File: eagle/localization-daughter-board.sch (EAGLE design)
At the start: 7 parts, among them U1 LM340MP-5.0/NOPB, U2 STM32F042FXP

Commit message: Just saving progress
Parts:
- added J2: (no value), SparkFun-Connectors:CONN_05JST-VERT
- added J3: (no value), Localization-Daughter-Board:CONN_03
- added U3: SN65HVD256DR, Localization-Daughter-Board:SN65HVD256DR
- added U4: TXS0101DCKR, Localization-Daughter-Board:TXS0101DCKR
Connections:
- new net DYN_OE: U4.OE
- new net N$2: J2.2, U3.CANH
- new net N$3: J2.3, U3.CANL
- new net UART_DYN_3V3: U4.A
- new net UART_DYN_5V: J3.3, U4.B
- net +12V: now also J2.5
- net +3V3: now also U3.VRXD, U4.VCCA
- net +5V: now also J2.1, U3.VCC, U4.VCCB
- net CAN_RX: now also U3.RXD
- net CAN_TX: now also U3.TXD
- net GND: now also J2.4, J3.1, U3.GND, U4.GND
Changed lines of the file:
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@@
 <part name="GND3" library="supply1" library_urn="urn:adsk.eagle:library:371" deviceset="GND" device=""/>
 <part name="J1" library="SparkFun-Connectors" deviceset="CONN_05" device=""/>
+<part name="J2" library="SparkFun-Connectors" deviceset="CONN_05" device="JST-VERT"/>
+<part name="U3" library="Localization-Daughter-Board" library_urn="urn:adsk.eagle:library:1230207" deviceset="SN65HVD256DR" device=""/>
+<part name="+3V2" library="supply1" library_urn="urn:adsk.eagle:library:371" deviceset="+3V3" device=""/>
+<part name="P+5" library="supply1" library_urn="urn:adsk.eagle:library:371" deviceset="+5V" device=""/>
+<part name="GND5" library="supply1" library_urn="urn:adsk.eagle:library:371" deviceset="GND" device=""/>
+<part name="J3" library="Localization-Daughter-Board" library_urn="urn:adsk.eagle:library:1230207" deviceset="CONN_03" device=""/>
+<part name="U4" library="Localization-Daughter-Board" library_urn="urn:adsk.eagle:library:1230207" deviceset="TXS0101DCKR" device="" package3d_urn="urn:adsk.eagle:package:1230550/1"/>
+<part name="P+6" library="supply1" library_urn="urn:adsk.eagle:library:371" deviceset="+5V" device=""/>
+<part name="+3V3" library="supply1" library_urn="urn:adsk.eagle:library:371" deviceset="+3V3" device=""/>
+<part name="P+4" library="supply1" library_urn="urn:adsk.eagle:library:371" deviceset="+12V" device=""/>
 </parts>
 <sheets>
@@
 <instance part="GND3" gate="1" x="137.16" y="68.58"/>
 <instance part="J1" gate="G$1" x="254" y="116.84" rot="R180"/>
+<instance part="J2" gate="G$1" x="243.84" y="177.8" rot="MR0"/>
+<instance part="U3" gate="A" x="175.26" y="172.72" rot="MR180"/>
+<instance part="+3V2" gate="G$1" x="220.98" y="185.42" smashed="yes">
+<attribute name="VALUE" x="217.17" y="186.69" size="1.778" layer="96"/>
+</instance>
+<instance part="P+5" gate="1" x="162.56" y="185.42" smashed="yes">
+<attribute name="VALUE" x="160.02" y="186.436" size="1.778" layer="96"/>
+</instance>
+<instance part="GND5" gate="1" x="162.56" y="167.64"/>
+<instance part="J3" gate="G$1" x="248.92" y="147.32" rot="R180"/>
+<instance part="U4" gate="A" x="185.42" y="147.32"/>
+<instance part="P+6" gate="1" x="220.98" y="152.4" smashed="yes">
+<attribute name="VALUE" x="217.17" y="153.67" size="1.778" layer="96"/>
+</instance>
+<instance part="+3V3" gate="G$1" x="185.42" y="152.4" smashed="yes">
+<attribute name="VALUE" x="181.61" y="153.67" size="1.778" layer="96"/>
+</instance>
+<instance part="P+4" gate="1" x="228.6" y="187.96" smashed="yes">
+<attribute name="VALUE" x="230.886" y="190.5" size="1.778" layer="96" rot="MR0"/>
+</instance>
 </instances>
 <busses>
@@
 <pinref part="U1" gate="A" pin="IN"/>
 <wire x1="48.26" y1="137.16" x2="50.8" y2="137.16" width="0.1524" layer="91"/>
+</segment>
+<segment>
+<pinref part="J2" gate="G$1" pin="5"/>
+<wire x1="236.22" y1="182.88" x2="228.6" y2="182.88" width="0.1524" layer="91"/>
+<pinref part="P+4" gate="1" pin="+12V"/>
+<wire x1="228.6" y1="182.88" x2="228.6" y2="185.42" width="0.1524" layer="91"/>
 </segment>
 </net>
@@
 <label x="236.22" y="119.38" size="1.778" layer="95"/>
 </segment>
+<segment>
+<pinref part="GND5" gate="1" pin="GND"/>
+<wire x1="162.56" y1="170.18" x2="162.56" y2="175.26" width="0.1524" layer="91"/>
+<pinref part="U3" gate="A" pin="GND"/>
+<wire x1="177.8" y1="175.26" x2="162.56" y2="175.26" width="0.1524" layer="91"/>
+</segment>
+<segment>
+<pinref part="J3" gate="G$1" pin="1"/>
+<wire x1="241.3" y1="149.86" x2="231.14" y2="149.86" width="0.1524" layer="91"/>
+<label x="236.22" y="149.86" size="1.778" layer="95" rot="MR0"/>
+</segment>
+<segment>
+<pinref part="U4" gate="A" pin="GND"/>
+<wire x1="187.96" y1="144.78" x2="167.64" y2="144.78" width="0.1524" layer="91"/>
+<label x="167.64" y="144.78" size="1.778" layer="95"/>
+</segment>
+<segment>
+<pinref part="J2" gate="G$1" pin="4"/>
+<wire x1="236.22" y1="180.34" x2="228.6" y2="180.34" width="0.1524" layer="91"/>
+<label x="228.6" y="180.34" size="1.778" layer="95"/>
+</segment>
 </net>
 <net name="+5V" class="0">
@@
 <junction x="99.06" y="78.74"/>
 </segment>
+<segment>
+<pinref part="P+5" gate="1" pin="+5V"/>
+<wire x1="162.56" y1="182.88" x2="162.56" y2="177.8" width="0.1524" layer="91"/>
+<pinref part="U3" gate="A" pin="VCC"/>
+<wire x1="177.8" y1="177.8" x2="162.56" y2="177.8" width="0.1524" layer="91"/>
+</segment>
+<segment>
+<pinref part="U4" gate="A" pin="VCCB"/>
+<wire x1="218.44" y1="147.32" x2="220.98" y2="147.32" width="0.1524" layer="91"/>
+<pinref part="P+6" gate="1" pin="+5V"/>
+<wire x1="220.98" y1="149.86" x2="220.98" y2="147.32" width="0.1524" layer="91"/>
+</segment>
+<segment>
+<pinref part="J2" gate="G$1" pin="1"/>
+<wire x1="236.22" y1="172.72" x2="228.6" y2="172.72" width="0.1524" layer="91"/>
+<label x="228.6" y="172.72" size="1.778" layer="95"/>
+</segment>
 </net>
 <net name="+3V3" class="0">
@@
 <wire x1="246.38" y1="121.92" x2="236.22" y2="121.92" width="0.1524" layer="91"/>
 <label x="236.22" y="121.92" size="1.778" layer="95"/>
+</segment>
+<segment>
+<pinref part="U3" gate="A" pin="VRXD"/>
+<wire x1="215.9" y1="180.34" x2="220.98" y2="180.34" width="0.1524" layer="91"/>
+<pinref part="+3V2" gate="G$1" pin="+3V3"/>
+<wire x1="220.98" y1="180.34" x2="220.98" y2="182.88" width="0.1524" layer="91"/>
+</segment>
+<segment>
+<pinref part="U4" gate="A" pin="VCCA"/>
+<wire x1="187.96" y1="147.32" x2="185.42" y2="147.32" width="0.1524" layer="91"/>
+<pinref part="+3V3" gate="G$1" pin="+3V3"/>
+<wire x1="185.42" y1="149.86" x2="185.42" y2="147.32" width="0.1524" layer="91"/>
 </segment>
 </net>
@@
 <label x="231.14" y="88.9" size="1.778" layer="95" rot="MR0"/>
 </segment>
+<segment>
+<pinref part="U3" gate="A" pin="TXD"/>
+<wire x1="177.8" y1="172.72" x2="167.64" y2="172.72" width="0.1524" layer="91"/>
+<label x="167.64" y="172.72" size="1.778" layer="95"/>
+</segment>
 </net>
 <net name="CAN_RX" class="0">
@@
 <label x="231.14" y="86.36" size="1.778" layer="95" rot="MR0"/>
 </segment>
+<segment>
+<pinref part="U3" gate="A" pin="RXD"/>
+<wire x1="177.8" y1="180.34" x2="167.64" y2="180.34" width="0.1524" layer="91"/>
+<label x="167.64" y="180.34" size="1.778" layer="95"/>
+</segment>
 </net>
 <net name="SDA1" class="0">
@@
 </segment>
 </net>
+<net name="N$2" class="0">
+<segment>
+<pinref part="J2" gate="G$1" pin="2"/>
+<pinref part="U3" gate="A" pin="CANH"/>
+<wire x1="236.22" y1="175.26" x2="215.9" y2="175.26" width="0.1524" layer="91"/>
+</segment>
+</net>
+<net name="N$3" class="0">
+<segment>
+<pinref part="J2" gate="G$1" pin="3"/>
+<pinref part="U3" gate="A" pin="CANL"/>
+<wire x1="236.22" y1="177.8" x2="215.9" y2="177.8" width="0.1524" layer="91"/>
+</segment>
+</net>
+<net name="UART_DYN_5V" class="0">
+<segment>
+<pinref part="J3" gate="G$1" pin="3"/>
+<wire x1="241.3" y1="144.78" x2="238.76" y2="144.78" width="0.1524" layer="91"/>
+<label x="236.22" y="142.24" size="1.778" layer="95" rot="MR0"/>
+<pinref part="U4" gate="A" pin="B"/>
+<wire x1="218.44" y1="142.24" x2="238.76" y2="142.24" width="0.1524" layer="91"/>
+<wire x1="238.76" y1="142.24" x2="238.76" y2="144.78" width="0.1524" layer="91"/>
+</segment>
+</net>
+<net name="DYN_OE" class="0">
+<segment>
+<pinref part="U4" gate="A" pin="OE"/>
+<wire x1="218.44" y1="144.78" x2="236.22" y2="144.78" width="0.1524" layer="91"/>
+<label x="236.22" y="144.78" size="1.778" layer="95" rot="MR0"/>
+</segment>
+</net>
+<net name="UART_DYN_3V3" class="0">
+<segment>
+<pinref part="U4" gate="A" pin="A"/>
+<wire x1="187.96" y1="142.24" x2="167.64" y2="142.24" width="0.1524" layer="91"/>
+<label x="167.64" y="142.24" size="1.778" layer="95"/>
+</segment>
+</net>

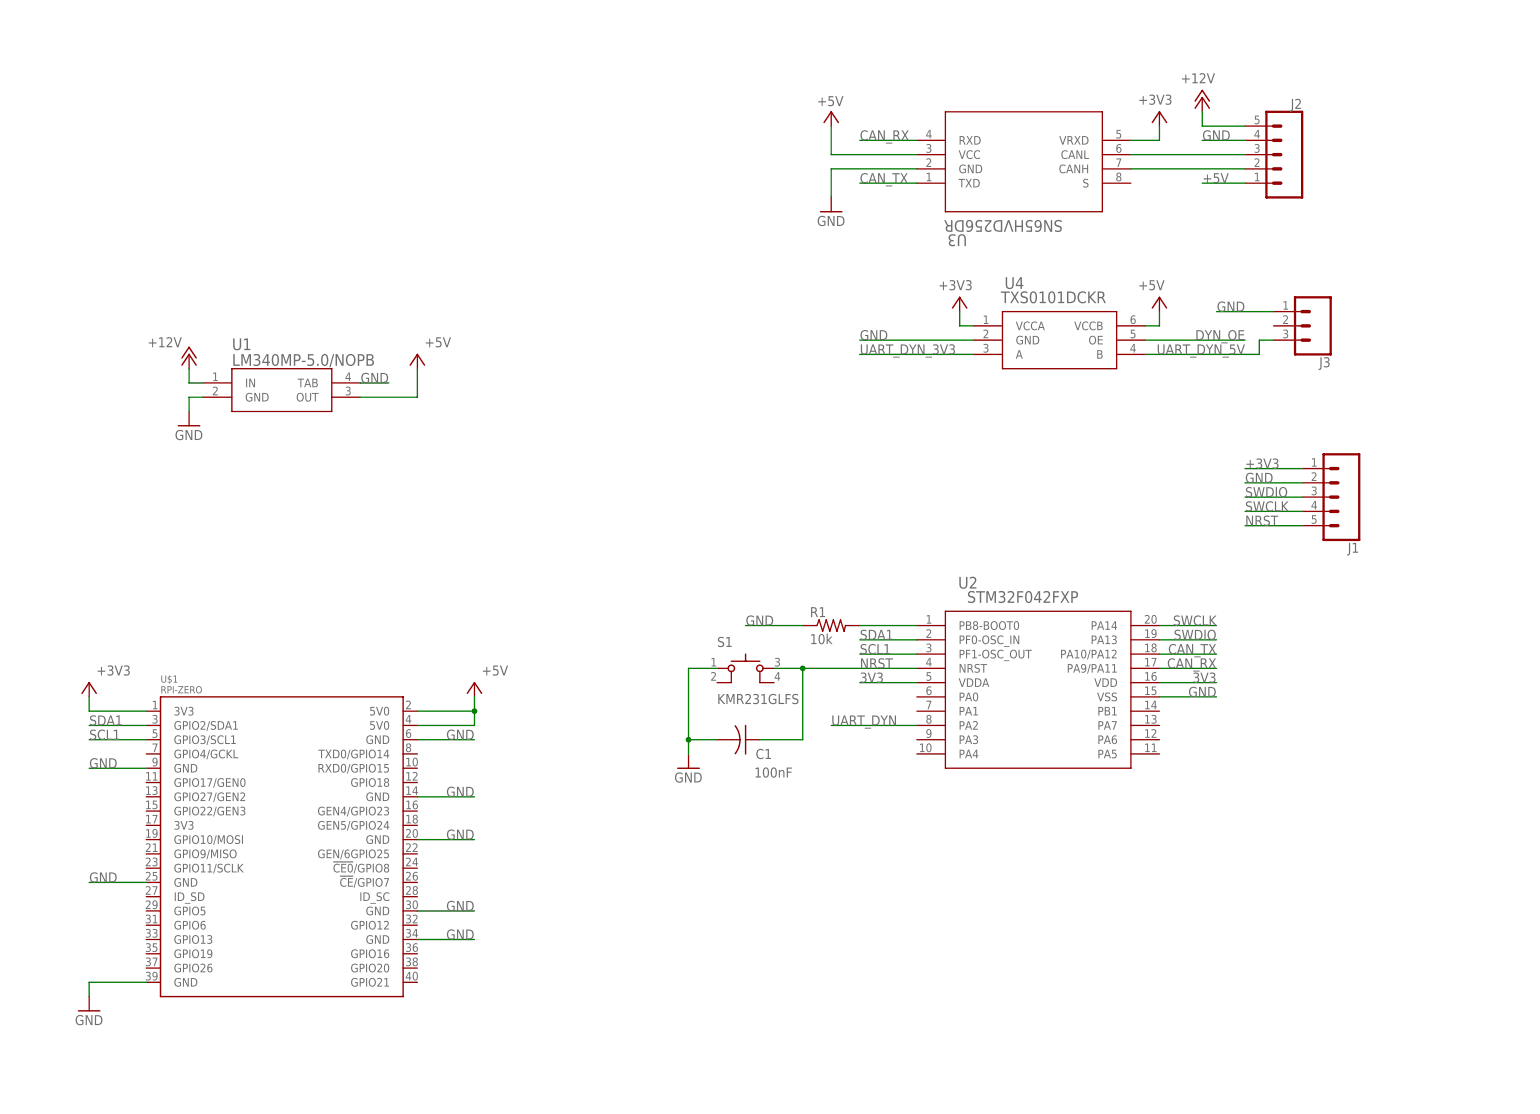
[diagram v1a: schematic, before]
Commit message: Finished initial schematic
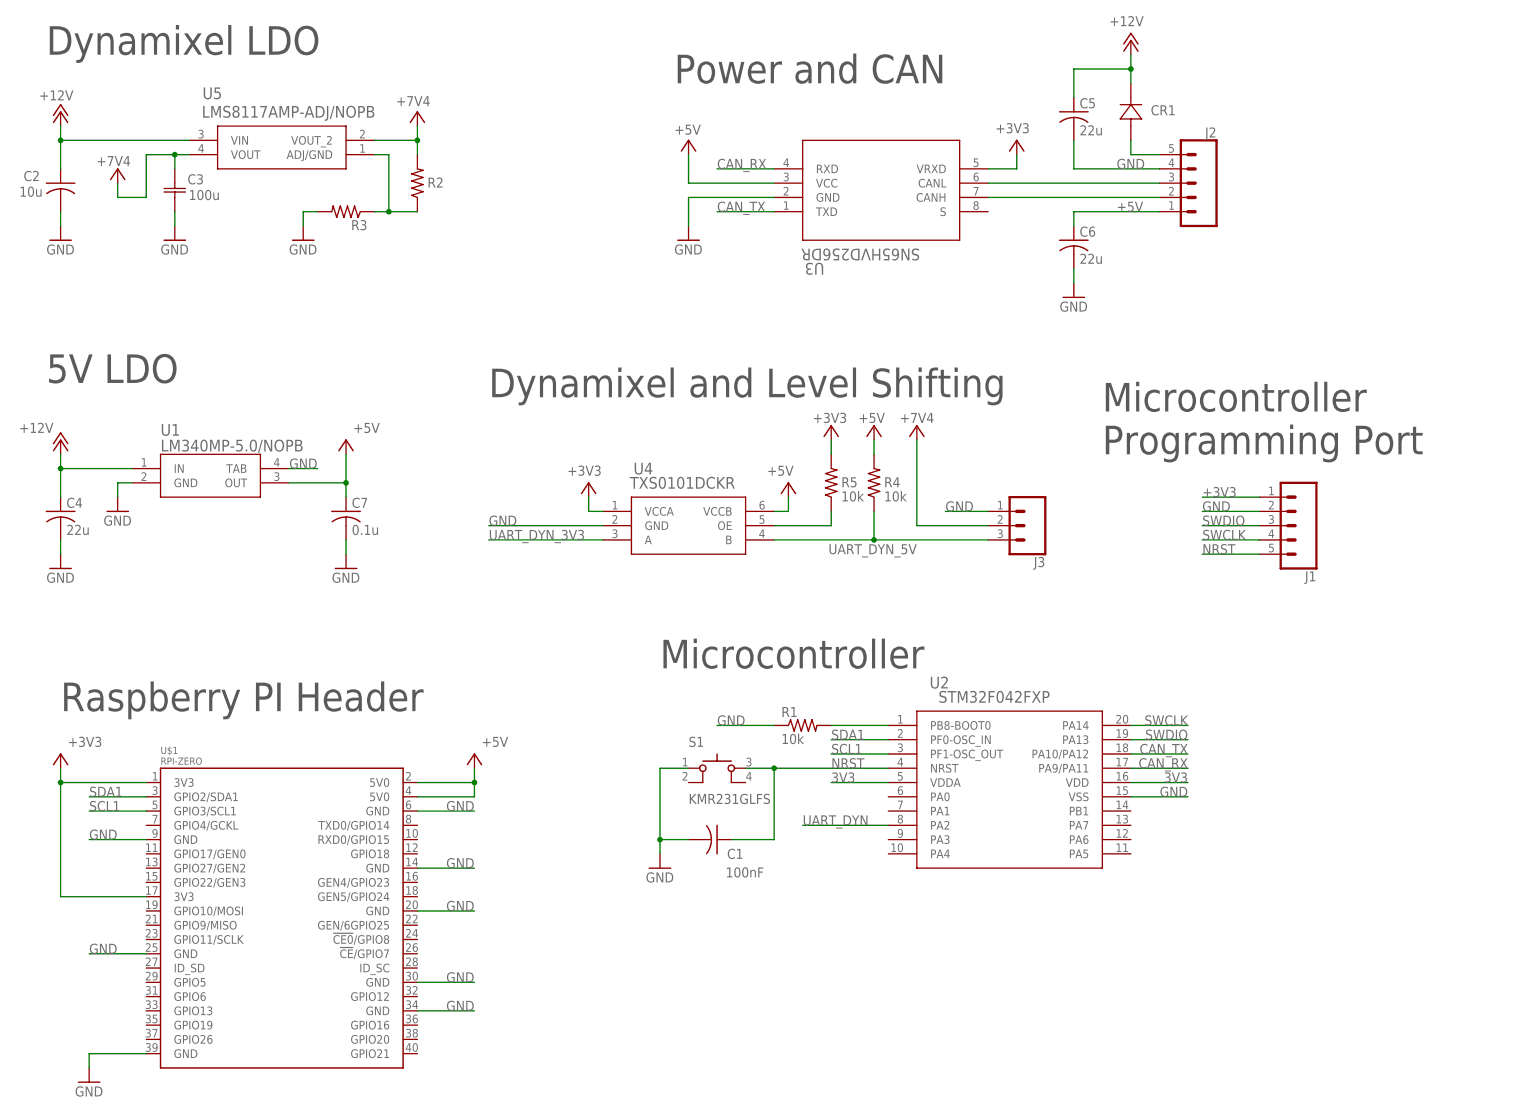
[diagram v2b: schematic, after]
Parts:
- added C2: 10u, resistor:C-USC1206
- added C3: 100u, Localization-Daughter-Board:F931C107MCC
- added C4, C5, C6: 22u, resistor:C-USC0805
- added C7: 0.1u, resistor:C-USC0805
- added CR1: STPS2H100A, Localization-Daughter-Board:STPS2H100A
- added R2, R3: (no value), resistor:R-US_R0805
- added R4, R5: 10k, resistor:R-US_R0805
- added U5: LMS8117AMP-ADJ/NOPB, Localization-Daughter-Board:LMS8117AMP-ADJ/NOPB
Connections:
- new net +7V4: C3.1, J3.2, R2.2, U5.VOUT, U5.VOUT_2
- new net N$4: R2.1, R3.1, U5.ADJ/GND
- new net N$5: CR1.22, J2.5
- net +12V: now also C2.1, C4.1, C5.1, CR1.11, U5.VIN; no longer J2.5
- net +3V3: now also R5.2, U$1.3V3@2
- net +5V: now also C6.1, C7.1, R4.2
- net DYN_OE: now also R5.1
- net GND: now also C2.2, C3.2, C4.2, C5.2, C6.2, C7.2, R3.2
- net UART_DYN_5V: now also R4.1
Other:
- note added: "5V LDO"
- note added: "Dynamixel LDO"
- note added: "Dynamixel and Level Shifting"
- note added: "Microcontroller"
- note added: "Microcontroller Programming Port"
- note added: "Power and CAN"
- note added: "Raspberry PI Header"
- moved on the sheet: C1, J1, J2, J3, R1, S1, U$1, U1, U2, U3, U4

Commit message: Fixed dynamixel connections
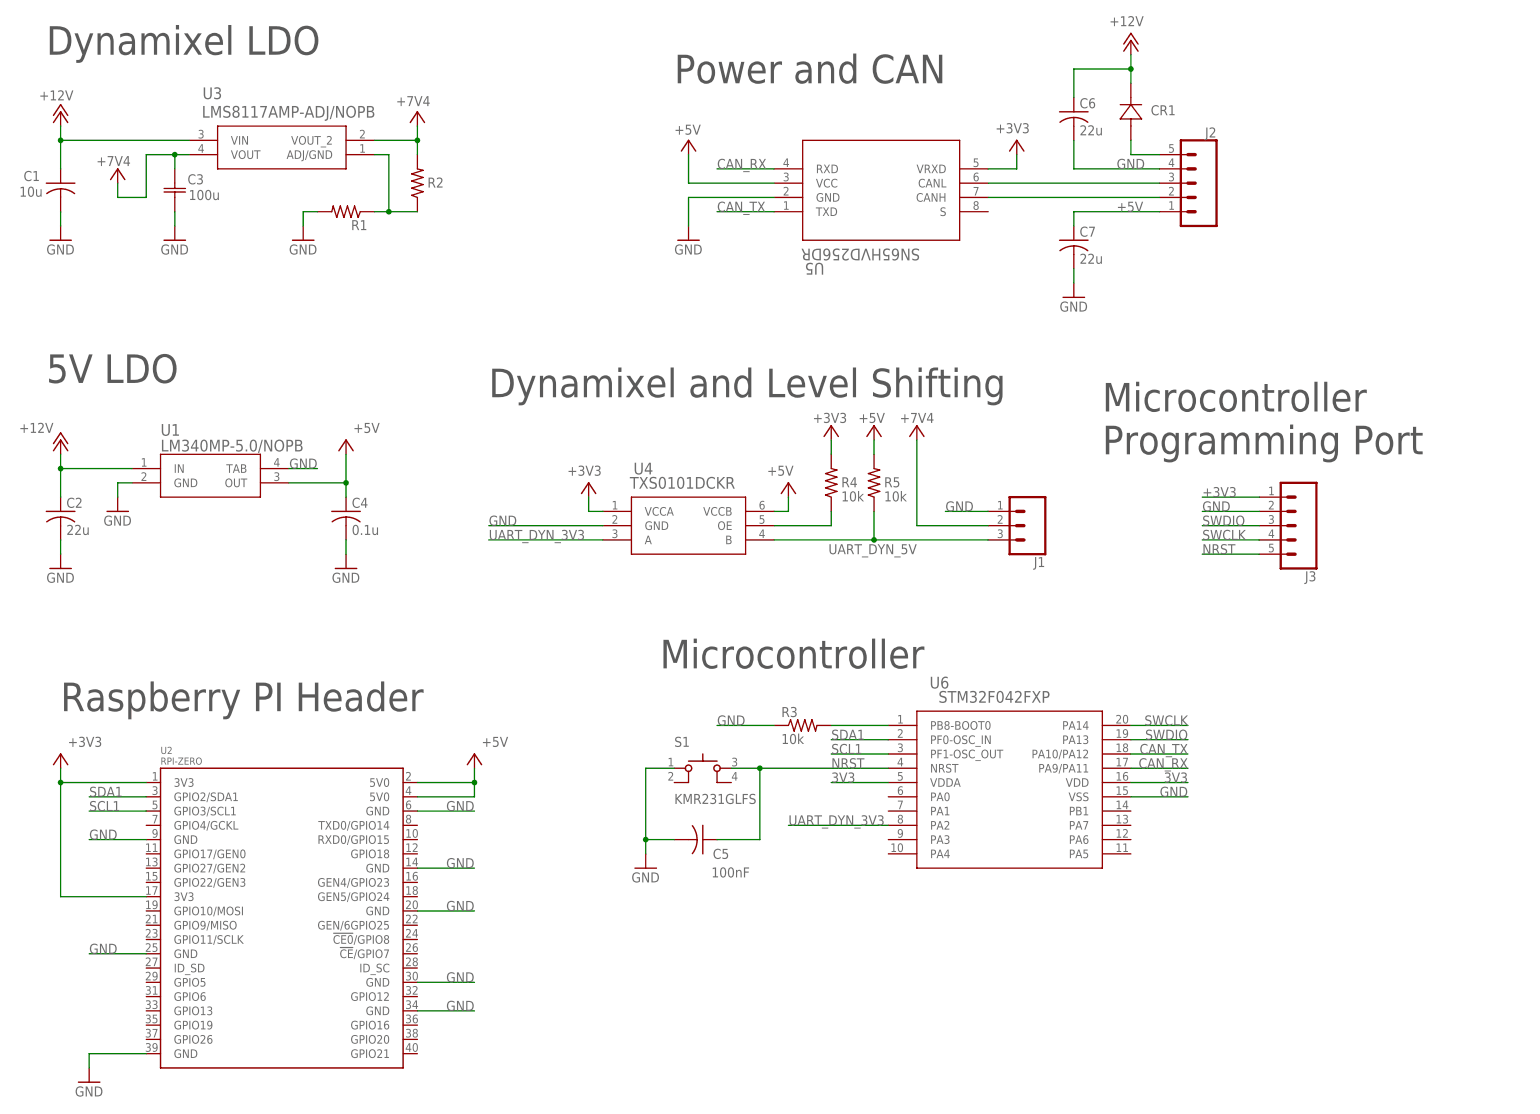
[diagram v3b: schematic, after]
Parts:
- removed U$1: RPI-ZERO, RPI-Zero:RPI-ZERO
- added U6: STM32F042FXP, Localization-Daughter-Board:STM32F042FXP
- C1: value 100nF -> 10u; device resistor:C-USC0805 -> resistor:C-USC1206
- C2: value 10u -> 22u; device resistor:C-USC1206 -> resistor:C-USC0805
- C4: value 22u -> 0.1u
- C5: value 22u -> 100nF
- C7: value 0.1u -> 22u
- J1: device SparkFun-Connectors:CONN_05 -> Localization-Daughter-Board:CONN_03
- J3: device Localization-Daughter-Board:CONN_03 -> SparkFun-Connectors:CONN_05
- R1: value 10k -> (none)
- R3: value (none) -> 10k
- U2: value STM32F042FXP -> RPI-ZERO; device Localization-Daughter-Board:STM32F042FXP -> RPI-Zero:RPI-ZERO
- U3: value SN65HVD256DR -> LMS8117AMP-ADJ/NOPB; device Localization-Daughter-Board:SN65HVD256DR -> Localization-Daughter-Board:LMS8117AMP-ADJ/NOPB
- U5: value LMS8117AMP-ADJ/NOPB -> SN65HVD256DR; device Localization-Daughter-Board:LMS8117AMP-ADJ/NOPB -> Localization-Daughter-Board:SN65HVD256DR
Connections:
- removed net UART_DYN: U2.PA2
- net +12V: now also C1.1, C6.1, U3.VIN; no longer C4.1, C5.1, U5.VIN
- net +3V3: now also J3.1, R4.2, U2.3V3@1, U2.3V3@2, U5.VRXD; no longer J1.1, R5.2, U$1.3V3@1, U$1.3V3@2, U3.VRXD
- net +5V: now also C4.1, R5.2, U2.5V0@1, U2.5V0@2, U5.VCC; no longer C6.1, R4.2, U$1.5V0@1, U$1.5V0@2, U3.VCC
- net +7V4: now also J1.2, U3.VOUT, U3.VOUT_2; no longer J3.2, U5.VOUT, U5.VOUT_2
- net 3V3: now also U6.VDD, U6.VDDA; no longer U2.VDD, U2.VDDA
- net CAN_RX: now also U5.RXD, U6.PA9/PA11; no longer U2.PA9/PA11, U3.RXD
- net CAN_TX: now also U5.TXD, U6.PA10/PA12; no longer U2.PA10/PA12, U3.TXD
- net DYN_OE: now also R4.1; no longer R5.1
- net GND: now also J1.1, J3.2, R1.2, R3.1, U2.GND@1, U2.GND@2, U2.GND@3, U2.GND@4, U2.GND@5, U2.GND@6, U2.GND@7, U2.GND@8, U5.GND, U6.VSS; no longer J1.2, J3.1, R1.1, R3.2, U$1.GND@1, U$1.GND@2, U$1.GND@3, U$1.GND@4, U$1.GND@5, U$1.GND@6, U$1.GND@7, U$1.GND@8, U2.VSS, U3.GND
- net N$1: now also R3.2, U6.PB8-BOOT0; no longer R1.2, U2.PB8-BOOT0
- net N$2: now also U5.CANH; no longer U3.CANH
- net N$3: now also U5.CANL; no longer U3.CANL
- net N$4: now also R1.1, U3.ADJ/GND; no longer R3.1, U5.ADJ/GND
- net NRST: now also C5.1, J3.5, U6.NRST; no longer C1.1, J1.5, U2.NRST
- net SCL1: now also U2.GPIO3/SCL1, U6.PF1-OSC_OUT; no longer U$1.GPIO3/SCL1, U2.PF1-OSC_OUT
- net SDA1: now also U2.GPIO2/SDA1, U6.PF0-OSC_IN; no longer U$1.GPIO2/SDA1, U2.PF0-OSC_IN
- net SWCLK: now also J3.4, U6.PA14; no longer J1.4, U2.PA14
- net SWDIO: now also J3.3, U6.PA13; no longer J1.3, U2.PA13
- net UART_DYN_3V3: now also U6.PA2
- net UART_DYN_5V: now also J1.3, R5.1; no longer J3.3, R4.1
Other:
- moved on the sheet: C1, C2, C4, C5, C6, C7, R1, R3, R4, R5, S1

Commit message: Finished initial power layout
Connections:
- net N$5 renamed VIN
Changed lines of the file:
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@@
 </segment>
 </net>
-<net name="N$5" class="0">
+<net name="VIN" class="0">
 <segment>
 <pinref part="J2" gate="G$1" pin="5"/>
